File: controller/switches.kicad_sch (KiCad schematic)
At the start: 6 parts, among them J4 Conn_01x08, J5 Conn_01x08, U1 74HC165, U2 74HC165

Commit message: Add test point.
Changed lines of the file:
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@@
+	(wire
+		(pts
+			(xy 162.56 73.66) (xy 162.56 72.39)
+		)
+		(stroke
+			(width 0)
+			(type default)
+		)
+	)
 	(wire
 		(pts
@@
 	(wire
 		(pts
-			(xy 154.94 73.66) (xy 140.97 73.66)
+			(xy 140.97 73.66) (xy 162.56 73.66)
 		)
 		(stroke
@@
 		)
 		(stroke
-			(width 0)
-			(type default)
-		)
-	)
-	(wire
-		(pts
-			(xy 154.94 69.85) (xy 154.94 73.66)
-		)
-		(stroke

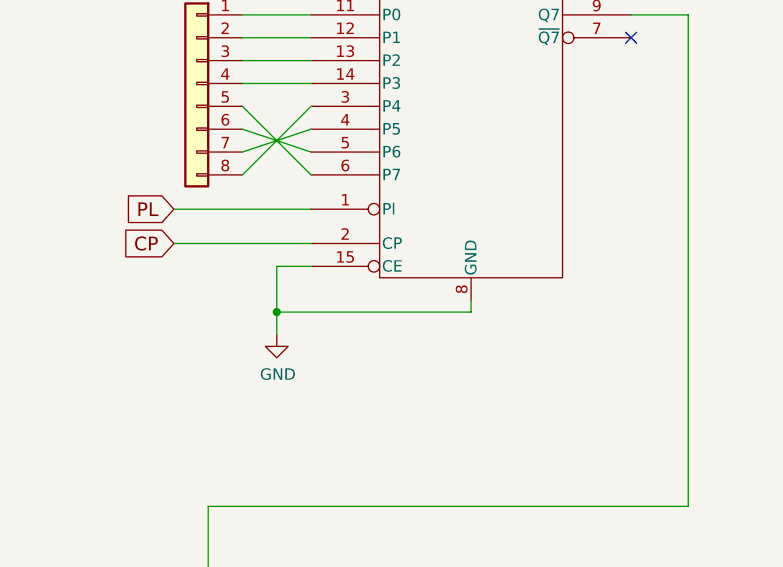
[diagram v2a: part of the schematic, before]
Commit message: Remove nRF24L01.
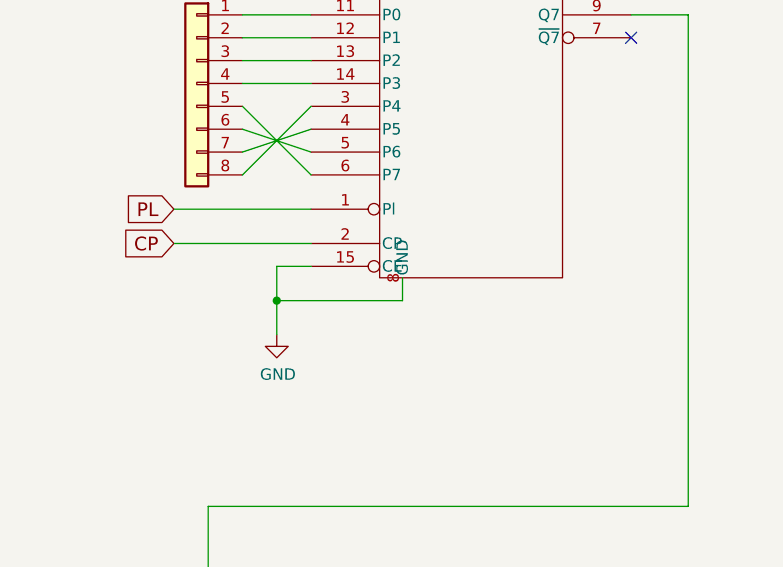
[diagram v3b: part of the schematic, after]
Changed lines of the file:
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@@
 (kicad_sch
-	(version 20240812)
+	(version 20241004)
 	(generator "eeschema")
 	(generator_version "8.99")
@@
 	)
 	(junction
+		(at 140.97 72.39)
+		(diameter 0)
+		(color 0 0 0 0)
+	)
+	(junction
 		(at 228.6 40.64)
 		(diameter 0)
@@
 		(color 0 0 0 0)
 	)
-	(junction
-		(at 140.97 73.66)
-		(diameter 0)
-		(color 0 0 0 0)
-	)
 	(no_connect
 		(at 172.72 127)
@@
 	(wire
 		(pts
-			(xy 140.97 73.66) (xy 140.97 68.58)
-		)
-		(stroke
-			(width 0)
-			(type default)
-		)
-	)
-	(wire
-		(pts
 			(xy 144.78 58.42) (xy 137.16 50.8)
 		)
@@
 	(wire
 		(pts
-			(xy 162.56 73.66) (xy 162.56 72.39)
-		)
-		(stroke
-			(width 0)
-			(type default)
-		)
-	)
-	(wire
-		(pts
 			(xy 137.16 53.34) (xy 144.78 55.88)
 		)
@@
 	(wire
 		(pts
+			(xy 140.97 72.39) (xy 140.97 76.2)
+		)
+		(stroke
+			(width 0)
+			(type default)
+		)
+	)
+	(wire
+		(pts
 			(xy 125.73 129.54) (xy 137.16 129.54)
 		)
@@
 	(wire
 		(pts
-			(xy 140.97 76.2) (xy 140.97 73.66)
+			(xy 140.97 68.58) (xy 140.97 72.39)
 		)
 		(stroke
@@
 	(wire
 		(pts
-			(xy 140.97 73.66) (xy 162.56 73.66)
+			(xy 154.94 72.39) (xy 140.97 72.39)
 		)
 		(stroke
@@
 		(pts
 			(xy 147.32 115.57) (xy 147.32 120.65)
+		)
+		(stroke
+			(width 0)
+			(type default)
+		)
+	)
+	(wire
+		(pts
+			(xy 154.94 69.85) (xy 154.94 72.39)
 		)
 		(stroke
@@
 			)
 		)
-		(property "Description" ""
+		(property "Description" "Shift Register 8 bits, parallel load"
 			(at 162.56 53.34 0)
 			(effects

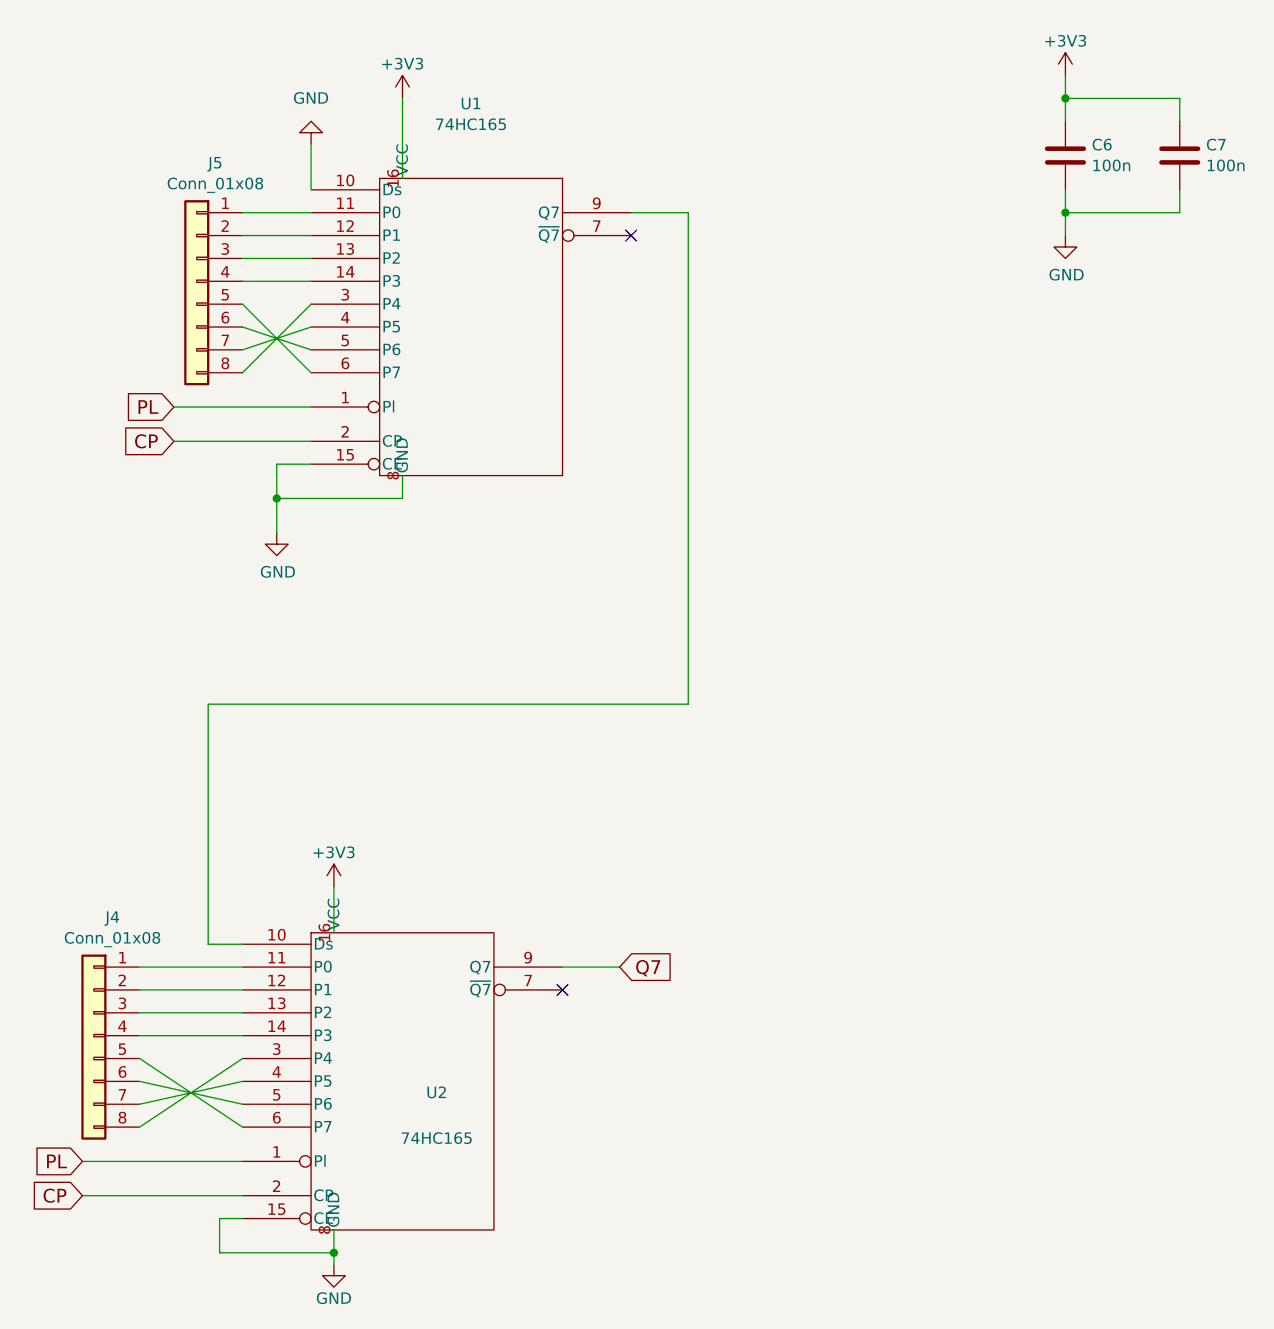
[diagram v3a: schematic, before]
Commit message: Power directly from battery.
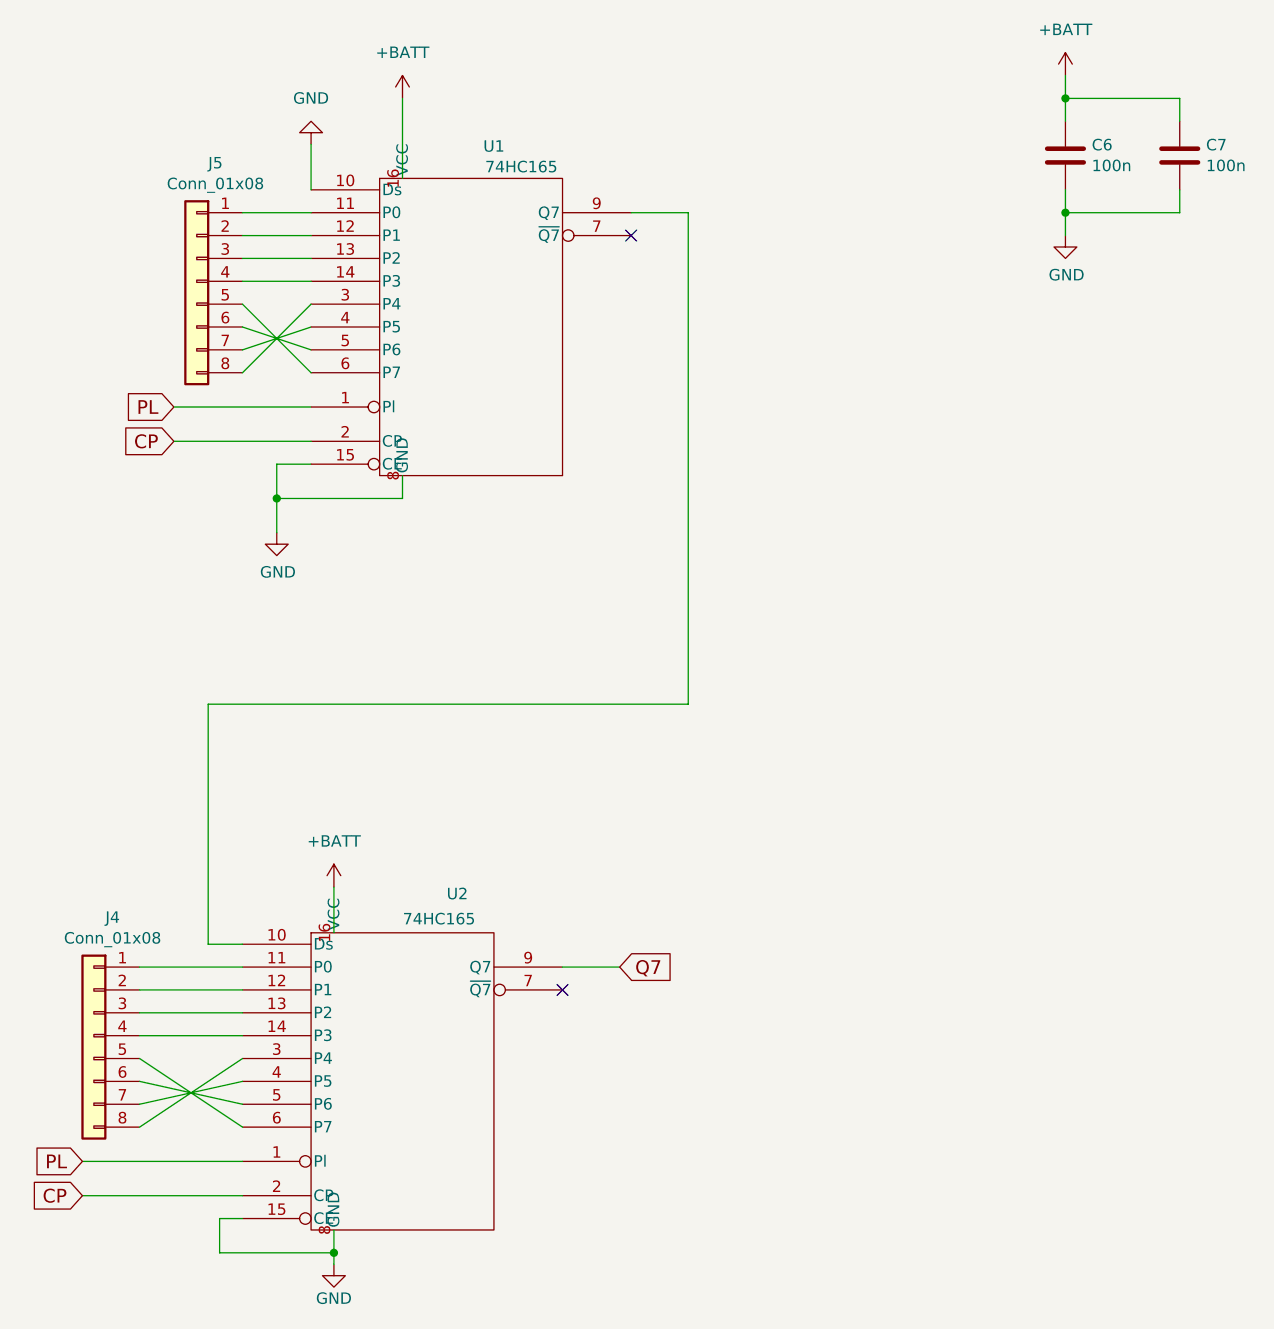
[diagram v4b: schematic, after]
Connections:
- net +3V3 renamed +BATT
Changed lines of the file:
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@@
 		(dnp no)
 		(property "Reference" "U2"
-			(at 158.75 138.43 0)
+			(at 161.036 116.332 0)
 			(effects
 				(font
@@
 		)
 		(property "Value" "74HC165"
-			(at 158.75 143.51 0)
+			(at 159.004 119.126 0)
 			(effects
 				(font
@@
 		(dnp no)
 		(property "Reference" "U1"
-			(at 162.56 28.5496 0)
+			(at 165.1 33.274 0)
 			(effects
 				(font
@@
 		)
 		(property "Value" "74HC165"
-			(at 162.56 30.861 0)
+			(at 168.148 35.56 0)
 			(effects
 				(font
@@
 	)
 	(symbol
-		(lib_id "power:+3V3")
+		(lib_id "power:+BATT")
 		(at 228.6 25.4 0)
 		(unit 1)
@@
 		(dnp no)
 		(fields_autoplaced yes)
-		(property "Reference" "#PWR022"
+		(property "Reference" "#PWR019"
 			(at 228.6 29.21 0)
 			(effects
@@
 			)
 		)
-		(property "Value" "+3V3"
-			(at 228.6 21.59 0)
+		(property "Value" "+BATT"
+			(at 228.6 20.32 0)
 			(effects
 				(font
@@
 			)
 		)
-		(property "Description" ""
+		(property "Description" "Power flag, positive battery voltage"
 			(at 228.6 25.4 0)
 			(effects
@@
 		)
 		(instances
-			(project "remote"
-				(path "/0776e334-fbf5-4a46-a47e-c7e0521e2a6b/00000000-0000-0000-0000-0000598770f9"
-					(reference "#PWR022")
-					(unit 1)
-				)
-			)
-		)
-	)
-	(symbol
-		(lib_id "power:+3V3")
+			(project ""
+				(path "/0776e334-fbf5-4a46-a47e-c7e0521e2a6b/00000000-0000-0000-0000-0000598770f9"
+					(reference "#PWR019")
+					(unit 1)
+				)
+			)
+		)
+	)
+	(symbol
+		(lib_id "power:+BATT")
+		(at 154.94 27.94 0)
+		(unit 1)
+		(exclude_from_sim no)
+		(in_bom yes)
+		(on_board yes)
+		(dnp no)
+		(fields_autoplaced yes)
+		(property "Reference" "#PWR018"
+			(at 154.94 31.75 0)
+			(effects
+				(font
+					(size 1.27 1.27)
+				)
+				(hide yes)
+			)
+		)
+		(property "Value" "+BATT"
+			(at 154.94 22.86 0)
+			(effects
+				(font
+					(size 1.27 1.27)
+				)
+			)
+		)
+		(property "Footprint" ""
+			(at 154.94 27.94 0)
+			(effects
+				(font
+					(size 1.27 1.27)
+				)
+				(hide yes)
+			)
+		)
+		(property "Datasheet" ""
+			(at 154.94 27.94 0)
+			(effects
+				(font
+					(size 1.27 1.27)
+				)
+				(hide yes)
+			)
+		)
+		(property "Description" "Power flag, positive battery voltage"
+			(at 154.94 27.94 0)
+			(effects
+				(font
+					(size 1.27 1.27)
+				)
+				(hide yes)
+			)
+		)
+		(pin "1"
+		)
+		(instances
+			(project ""
+				(path "/0776e334-fbf5-4a46-a47e-c7e0521e2a6b/00000000-0000-0000-0000-0000598770f9"
+					(reference "#PWR018")
+					(unit 1)
+				)
+			)
+		)
+	)
+	(symbol
+		(lib_id "power:+BATT")
 		(at 147.32 115.57 0)
 		(unit 1)
@@
 		(dnp no)
 		(fields_autoplaced yes)
-		(property "Reference" "#PWR021"
+		(property "Reference" "#PWR020"
 			(at 147.32 119.38 0)
 			(effects
@@
 			)
 		)
-		(property "Value" "+3V3"
-			(at 147.32 111.76 0)
+		(property "Value" "+BATT"
+			(at 147.32 110.49 0)
 			(effects
 				(font
@@
 			)
 		)
-		(property "Description" ""
+		(property "Description" "Power flag, positive battery voltage"
 			(at 147.32 115.57 0)
 			(effects
@@
 		)
 		(instances
-			(project "remote"
-				(path "/0776e334-fbf5-4a46-a47e-c7e0521e2a6b/00000000-0000-0000-0000-0000598770f9"
-					(reference "#PWR021")
+			(project ""
+				(path "/0776e334-fbf5-4a46-a47e-c7e0521e2a6b/00000000-0000-0000-0000-0000598770f9"
+					(reference "#PWR020")
 					(unit 1)
 				)
@@
 					(unit 1)
 				)
-			)
-		)
-	)
-	(symbol
-		(lib_id "power:+3V3")
-		(at 154.94 27.94 0)
-		(unit 1)
-		(exclude_from_sim no)
-		(in_bom yes)
-		(on_board yes)
-		(dnp no)
-		(fields_autoplaced yes)
-		(property "Reference" "#PWR020"
-			(at 154.94 31.75 0)
-			(effects
-				(font
-					(size 1.27 1.27)
-				)
-				(hide yes)
-			)
-		)
-		(property "Value" "+3V3"
-			(at 154.94 24.13 0)
-			(effects
-				(font
-					(size 1.27 1.27)
-				)
-			)
-		)
-		(property "Footprint" ""
-			(at 154.94 27.94 0)
-			(effects
-				(font
-					(size 1.27 1.27)
-				)
-				(hide yes)
-			)
-		)
-		(property "Datasheet" ""
-			(at 154.94 27.94 0)
-			(effects
-				(font
-					(size 1.27 1.27)
-				)
-				(hide yes)
-			)
-		)
-		(property "Description" ""
-			(at 154.94 27.94 0)
-			(effects
-				(font
-					(size 1.27 1.27)
-				)
-				(hide yes)
-			)
-		)
-		(pin "1"
-		)
-		(instances
-			(project "remote"
-				(path "/0776e334-fbf5-4a46-a47e-c7e0521e2a6b/00000000-0000-0000-0000-0000598770f9"
-					(reference "#PWR020")
-					(unit 1)
-				)
